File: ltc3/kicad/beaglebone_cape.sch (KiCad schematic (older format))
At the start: 8 parts, among them U501 24C256

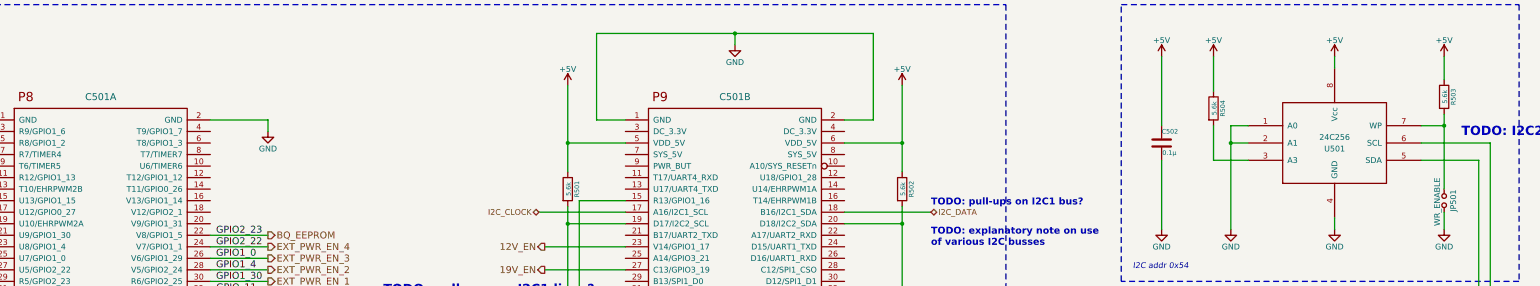
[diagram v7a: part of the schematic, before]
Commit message: LTC3: Replaced 2-cell battery symbol with 1-cell symbol.
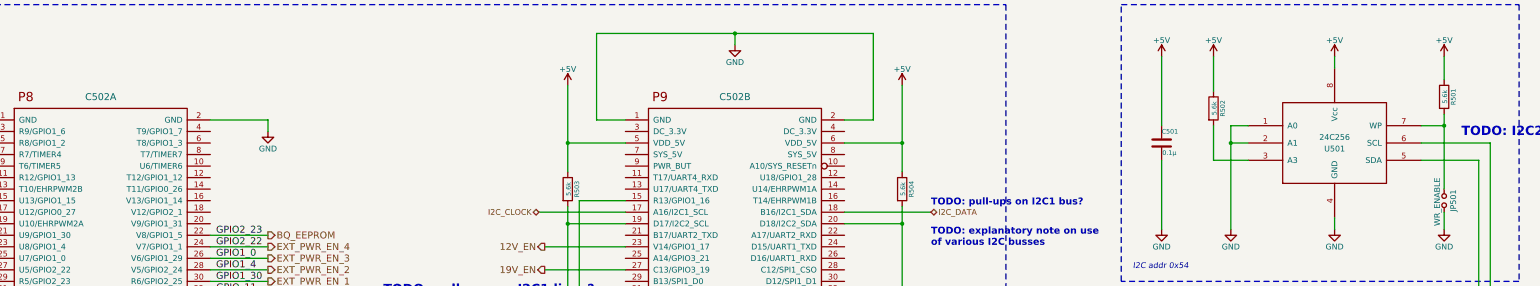
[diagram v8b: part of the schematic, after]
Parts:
- renumbered C501 to C502, R503 to R501, R504 to R502, R501 to R503, R502 to R504
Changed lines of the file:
@@
 LIBS:NDS9407
 LIBS:PI2127
+LIBS:battery_single_cell
+LIBS:Launch_Tower_Computer_III-cache
 EELAYER 25 0
 EELAYER END
@@
 P 12650 3550
 AR Path="/55052668" Ref="C502"  Part="1"
-AR Path="/55051BA8/55052668" Ref="C502"  Part="1"
-F 0 "C502" H 12650 3650 40  0000 L CNN
+AR Path="/55051BA8/55052668" Ref="C501"  Part="1"
+F 0 "C501" H 12650 3650 40  0000 L CNN
 F 1 "0.1μ" H 12656 3465 40  0000 L CNN
 F 2 "~" H 12688 3400 30  0000 C CNN
@@
 $EndComp
 $Comp
-L R R504
+L R R502
 U 1 1 55052963
 P 13100 3250
-F 0 "R504" V 13180 3250 40  0000 C CNN
+F 0 "R502" V 13180 3250 40  0000 C CNN
 F 1 "5.6k" V 13107 3251 40  0000 C CNN
 F 2 "~" V 13030 3250 30  0000 C CNN
@@
 $EndComp
 $Comp
-L R R503
+L R R501
 U 1 1 55052990
 P 15100 3150
-F 0 "R503" V 15180 3150 40  0000 C CNN
+F 0 "R501" V 15180 3150 40  0000 C CNN
 F 1 "5.6k" V 15107 3151 40  0000 C CNN
 F 2 "~" V 15030 3150 30  0000 C CNN
@@
 EXT_PWR_EN_4
 $Comp
-L GND #PWR514
+L GND #PWR512
 U 1 1 557C941A
 P 14150 4300
-F 0 "#PWR514" H 14150 4050 50  0001 C CNN
+F 0 "#PWR512" H 14150 4050 50  0001 C CNN
 F 1 "GND" H 14150 4150 50  0000 C CNN
 F 2 "" H 14150 4300 60  0000 C CNN
@@
 $EndComp
 $Comp
-L GND #PWR515
+L GND #PWR513
 U 1 1 557CCCE2
 P 15100 4300
-F 0 "#PWR515" H 15100 4050 50  0001 C CNN
+F 0 "#PWR513" H 15100 4050 50  0001 C CNN
 F 1 "GND" H 15100 4150 50  0000 C CNN
 F 2 "" H 15100 4300 60  0000 C CNN
@@
 $EndComp
 $Comp
-L GND #PWR513
+L GND #PWR511
 U 1 1 557CCE7C
 P 13250 4300
-F 0 "#PWR513" H 13250 4050 50  0001 C CNN
+F 0 "#PWR511" H 13250 4050 50  0001 C CNN
 F 1 "GND" H 13250 4150 50  0000 C CNN
 F 2 "" H 13250 4300 60  0000 C CNN
@@
 $EndComp
 $Comp
-L GND #PWR512
+L GND #PWR510
 U 1 1 557CE60A
 P 12650 4300
-F 0 "#PWR512" H 12650 4050 50  0001 C CNN
+F 0 "#PWR510" H 12650 4050 50  0001 C CNN
 F 1 "GND" H 12650 4150 50  0000 C CNN
 F 2 "" H 12650 4300 60  0000 C CNN
@@
 	2000 4950 2500 4950
 $Comp
-L BeagleBone_Black_Expansion_Header C501
+L BeagleBone_Black_Expansion_Header C502
 U 1 1 55E6D53E
 P 3450 4350
-F 0 "C501" H 3450 5550 60  0000 C CNN
+F 0 "C502" H 3450 5550 60  0000 C CNN
 F 1 "BeagleBone_Black_Expansion_Header" H 3450 2950 60  0000 C CNN
 F 2 "" H 3450 4350 60  0000 C CNN
@@
 $EndComp
 $Comp
-L BeagleBone_Black_Expansion_Header C501
+L BeagleBone_Black_Expansion_Header C502
 U 2 1 55E6D67B
 P 8950 4350
-F 0 "C501" H 8950 5550 60  0000 C CNN
+F 0 "C502" H 8950 5550 60  0000 C CNN
 F 1 "BeagleBone_Black_Expansion_Header" H 8950 2950 60  0000 C CNN
 F 2 "" H 8950 4350 60  0000 C CNN
@@
 	2500 4850 2000 4850
 $Comp
-L GND #PWR504
+L GND #PWR508
 U 1 1 55E75ADE
 P 2000 3450
-F 0 "#PWR504" H 2000 3200 50  0001 C CNN
+F 0 "#PWR508" H 2000 3200 50  0001 C CNN
 F 1 "GND" H 2000 3300 50  0000 C CNN
 F 2 "" H 2000 3450 60  0000 C CNN
@@
 	2000 3350 2500 3350
 $Comp
-L GND #PWR505
+L GND #PWR509
 U 1 1 55E75BB5
 P 4900 3450
-F 0 "#PWR505" H 4900 3200 50  0001 C CNN
+F 0 "#PWR509" H 4900 3200 50  0001 C CNN
 F 1 "GND" H 4900 3300 50  0000 C CNN
 F 2 "" H 4900 3450 60  0000 C CNN
@@
 	4900 3350 4400 3350
 $Comp
-L GND #PWR506
+L GND #PWR514
 U 1 1 55E77963
 P 7750 5650
-F 0 "#PWR506" H 7750 5400 50  0001 C CNN
+F 0 "#PWR514" H 7750 5400 50  0001 C CNN
 F 1 "GND" H 7750 5500 50  0000 C CNN
 F 2 "" H 7750 5650 60  0000 C CNN
@@
 Connection ~ 7750 5550
 $Comp
-L GND #PWR507
+L GND #PWR515
 U 1 1 55E77AD2
 P 10150 5650
-F 0 "#PWR507" H 10150 5400 50  0001 C CNN
+F 0 "#PWR515" H 10150 5400 50  0001 C CNN
 F 1 "GND" H 10150 5500 50  0000 C CNN
 F 2 "" H 10150 5650 60  0000 C CNN
@@
 /ROCKET_READY
 $Comp
-L +5V #PWR503
+L +5V #PWR507
 U 1 1 565530F5
 P 10400 3050
-F 0 "#PWR503" H 10400 2900 50  0001 C CNN
+F 0 "#PWR507" H 10400 2900 50  0001 C CNN
 F 1 "+5V" H 10400 3190 50  0000 C CNN
 F 2 "" H 10400 3050 60  0000 C CNN
@@
 	10400 3050 10400 3800
 $Comp
-L +5V #PWR502
+L +5V #PWR506
 U 1 1 565538D1
 P 7500 3050
-F 0 "#PWR502" H 7500 2900 50  0001 C CNN
+F 0 "#PWR506" H 7500 2900 50  0001 C CNN
 F 1 "+5V" H 7500 3190 50  0000 C CNN
 F 2 "" H 7500 3050 60  0000 C CNN
@@
 	7500 3050 7500 3800
 $Comp
-L +5V #PWR508
+L +5V #PWR502
 U 1 1 56555506
 P 12650 2800
-F 0 "#PWR508" H 12650 2650 50  0001 C CNN
+F 0 "#PWR502" H 12650 2650 50  0001 C CNN
 F 1 "+5V" H 12650 2940 50  0000 C CNN
 F 2 "" H 12650 2800 60  0000 C CNN
@@
 $EndComp
 $Comp
-L +5V #PWR509
+L +5V #PWR503
 U 1 1 56555577
 P 13100 2800
-F 0 "#PWR509" H 13100 2650 50  0001 C CNN
+F 0 "#PWR503" H 13100 2650 50  0001 C CNN
 F 1 "+5V" H 13100 2940 50  0000 C CNN
 F 2 "" H 13100 2800 60  0000 C CNN
@@
 $EndComp
 $Comp
-L +5V #PWR510
+L +5V #PWR504
 U 1 1 565555AF
 P 14150 2800
-F 0 "#PWR510" H 14150 2650 50  0001 C CNN
+F 0 "#PWR504" H 14150 2650 50  0001 C CNN
 F 1 "+5V" H 14150 2940 50  0000 C CNN
 F 2 "" H 14150 2800 60  0000 C CNN
@@
 $EndComp
 $Comp
-L +5V #PWR511
+L +5V #PWR505
 U 1 1 565555E7
 P 15100 2800
-F 0 "#PWR511" H 15100 2650 50  0001 C CNN
+F 0 "#PWR505" H 15100 2650 50  0001 C CNN
 F 1 "+5V" H 15100 2940 50  0000 C CNN
 F 2 "" H 15100 2800 60  0000 C CNN
@@
 I2C addr 0x54
 $Comp
-L R R502
+L R R504
 U 1 1 5658AA1A
 P 10400 3950
-F 0 "R502" V 10480 3950 40  0000 C CNN
+F 0 "R504" V 10480 3950 40  0000 C CNN
 F 1 "5.6k" V 10407 3951 40  0000 C CNN
 F 2 "~" V 10330 3950 30  0000 C CNN
@@
 $EndComp
 $Comp
-L R R501
+L R R503
 U 1 1 5658AFE1
 P 7500 3950
-F 0 "R501" V 7580 3950 40  0000 C CNN
+F 0 "R503" V 7580 3950 40  0000 C CNN
 F 1 "5.6k" V 7507 3951 40  0000 C CNN
 F 2 "~" V 7430 3950 30  0000 C CNN
